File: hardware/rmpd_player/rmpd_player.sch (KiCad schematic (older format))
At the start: 63 parts, among them J1 POWER, J2 PROG, J3 LINE_OUT_INT, J4 LINE_OUT, J5 MICRO_SD, J6 POWER_INT, Q1 BC848, Q2 BC848, Q3 BC858, Q4 BC858, U1 DS3231M, U2 VS1011E, U3 LM1117-3.3, U4 ESP32-WROOM, Y1 12.288MHz

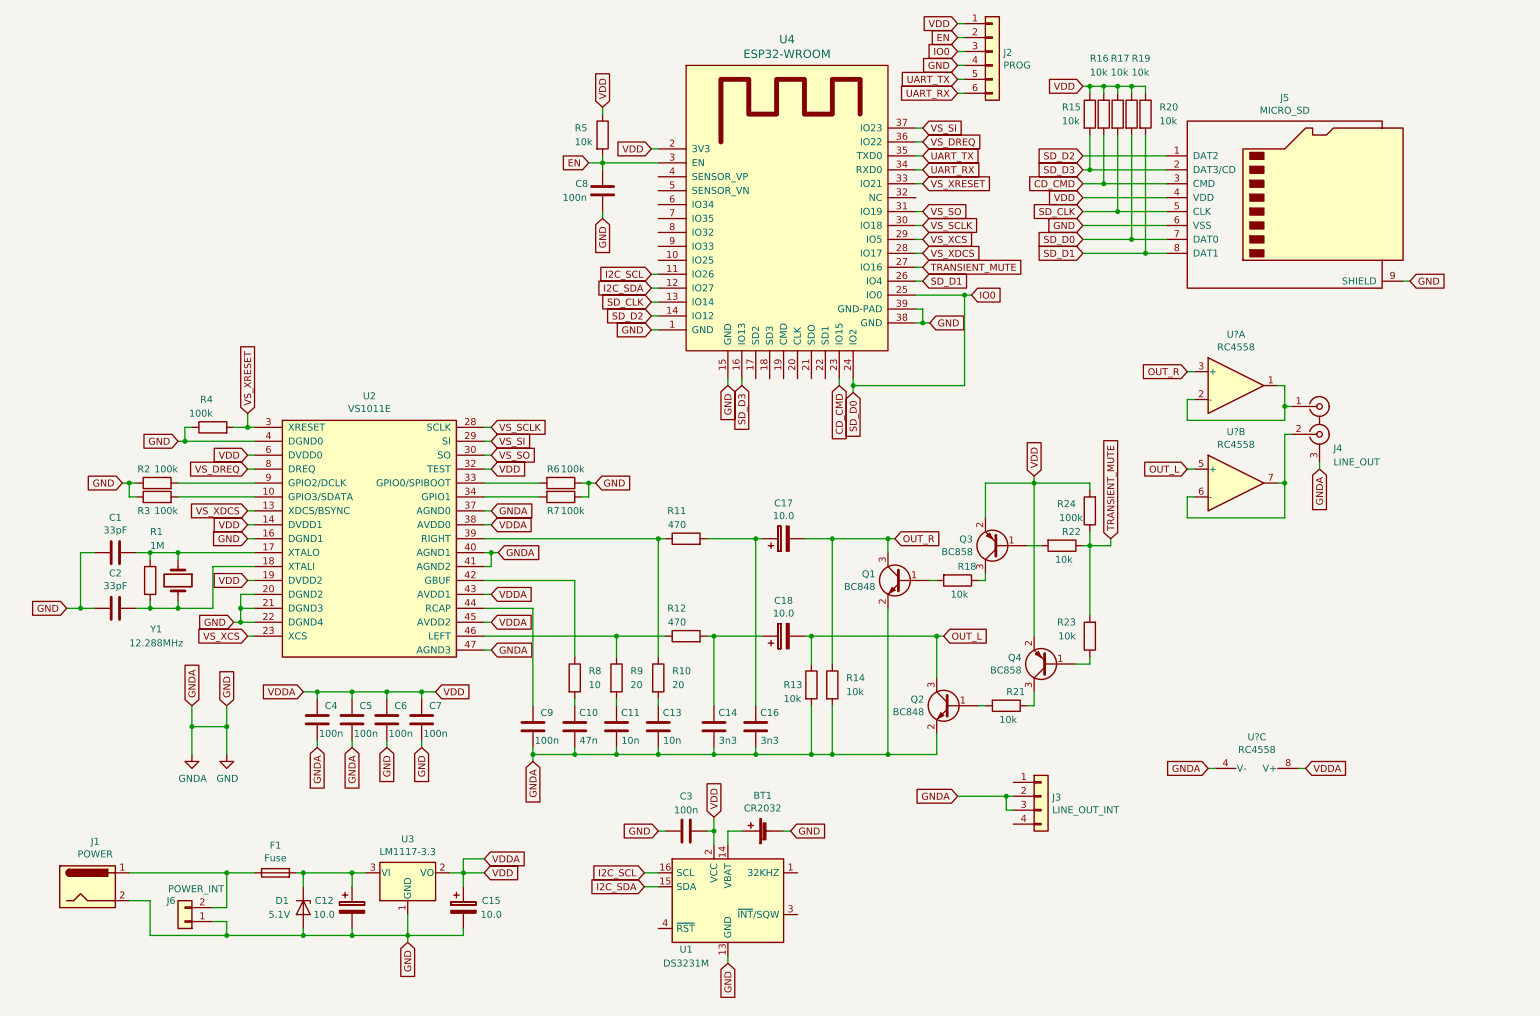
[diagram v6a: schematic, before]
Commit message: schematic op amp buffer; bom list
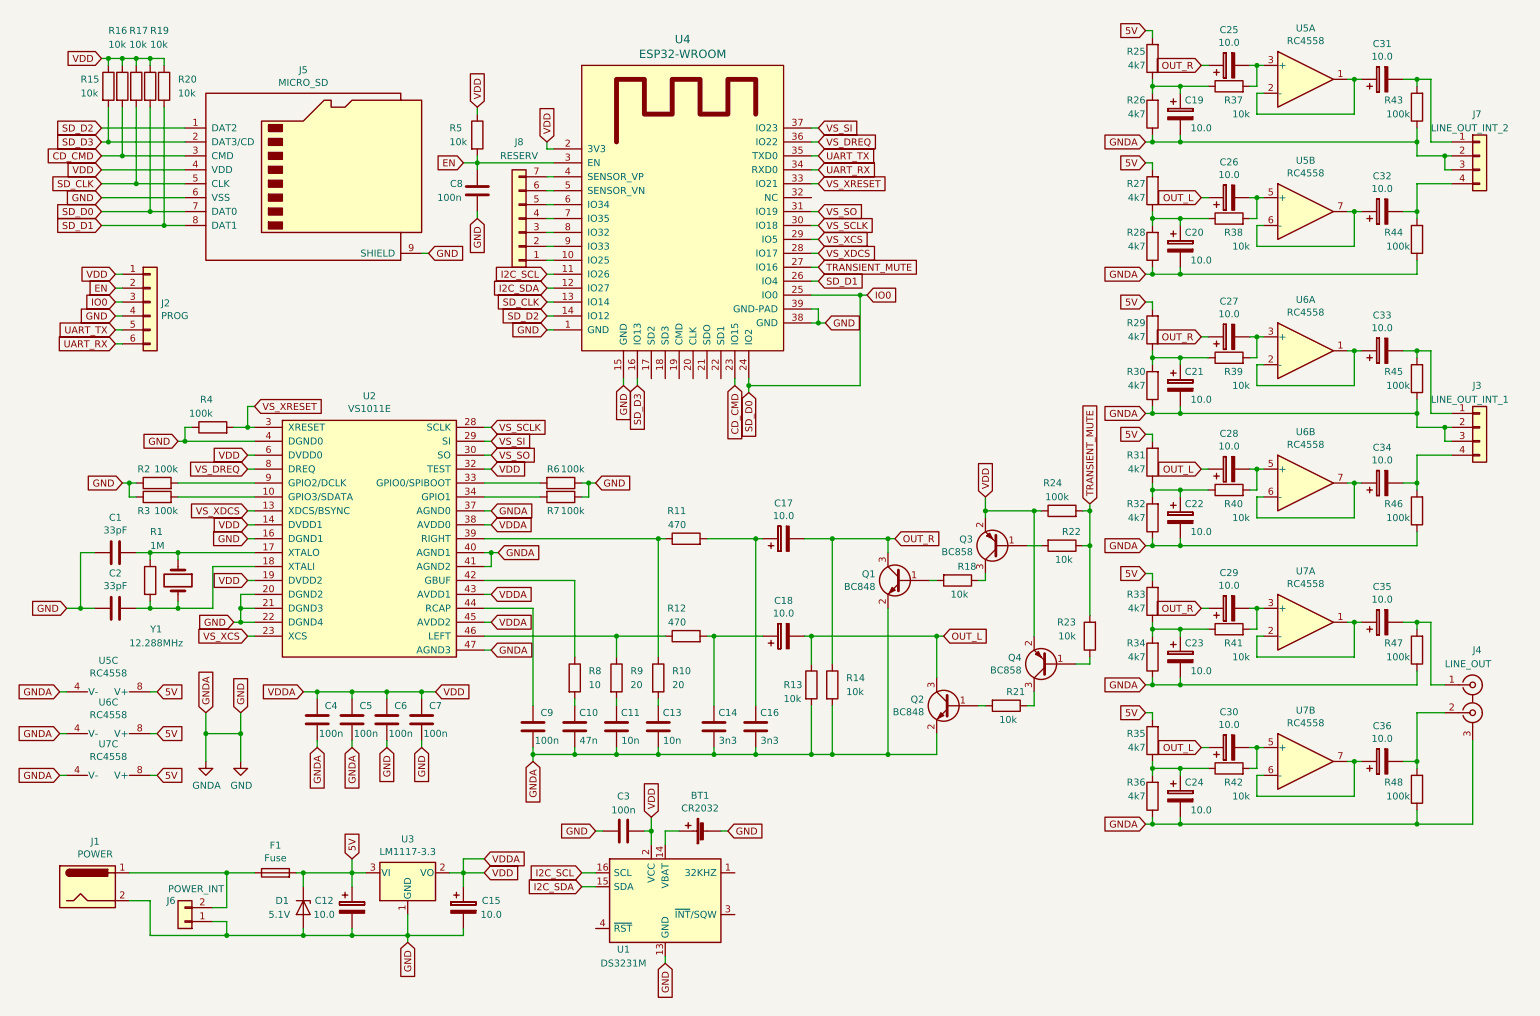
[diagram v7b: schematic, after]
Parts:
- added C19, C20, C21, C22, C23, C24, C25, C26, C27, C28, C29, C30, C31, C32, C33, C34, C35, C36: 10.0, Capacitors_THT:CP_Radial_D5.0mm_P2.50mm, symbol Device:CP
- added J7: LINE_OUT_INT_2, Pin_Headers:Pin_Header_Straight_1x04_Pitch2.54mm, symbol Connector_Generic:Conn_01x04
- added J8: RESERV, Pin_Headers:Pin_Header_Straight_1x07_Pitch2.54mm, symbol Connector_Generic:Conn_01x07
- added R25, R26, R27, R28, R29, R30, R31, R32, R33, R34, R35, R36: 4k7, Resistors_SMD:R_0805_HandSoldering, symbol Device:R
- added R37, R38, R39, R40, R41, R42: 10k, Resistors_SMD:R_0805_HandSoldering, symbol Device:R
- added R43, R44, R45, R46, R47, R48: 100k, Resistors_SMD:R_0805_HandSoldering, symbol Device:R
- added unit 1 of U5
- added unit 2 of U5
- added U6: RC4558, Power_Integrations:SO-8, symbol Amplifier_Operational:RC4558
- added unit 3 of U7
- J3: value LINE_OUT_INT -> LINE_OUT_INT_1
- U5, U7: renamed from U?; footprint (none) -> Power_Integrations:SO-8
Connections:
- net GND: now also C19.2, C20.2, C21.2, C22.2, C23.2, C24.2, J7.2 (Pin_2), J7.3 (Pin_3), R26.1, R28.1, R30.1, R32.1, R34.1, R36.1, R43.1, R44.1, R45.1, R46.1, R47.1, R48.1, U6.4 (V-), U7.4 (V-)
- net OUT_L: now also C26.1, C28.1, C30.1; no longer U7.5 (+)
- net OUT_R: now also C25.1, C27.1, C29.1; no longer U7.3 (+)
- net TRANSIENT_MUTE: now also R24.2; no longer R24.1
- net VDD: now also R24.1; no longer R24.2, U5.8 (V+)
- net at U4.10 (IO25): now also J8.1 (Pin_1)
- net at U4.4 (SENSOR_VP): now also J8.7 (Pin_7)
- net at U4.5 (SENSOR_VN): now also J8.6 (Pin_6)
- net at U4.6 (IO34): now also J8.5 (Pin_5)
- net at U4.7 (IO35): now also J8.4 (Pin_4)
- net at U4.8 (IO32): now also J8.3 (Pin_3)
- net at U4.9 (IO33): now also J8.2 (Pin_2)
- net 5V: now reaches C12.1, D1.1 (K), F1.2, U3.3 (VI)
- net 5V: now also U5.8 (V+), R25.2, R27.2, R29.2, R31.2, R33.2, R35.2, U6.8 (V+), U7.8 (V+)
- net at U7.1, U7.2 (-): now also C35.1; no longer J4.1 (IN1)
- net at U7.6 (-), U7.7: now also C36.1; no longer J4.2 (IN2)
- net at J3.1 (Pin_1): now also C33.2, R45.2
- net at J3.4 (Pin_4): now also C34.2, R46.2
- new net: C35.2, J4.1 (IN1), R47.2
- new net: C36.2, J4.2 (IN2), R48.2
- new net: C29.2, R41.2, U7.3 (+)
- new net: C30.2, R42.2, U7.5 (+)
- new net: C23.1, R33.1, R34.2, R41.1
- new net: C24.1, R35.1, R36.2, R42.1
- new net: C33.1, U6.1, U6.2 (-)
- new net: C27.2, R39.2, U6.3 (+)
- new net: C28.2, R40.2, U6.5 (+)
- new net: C34.1, U6.6 (-), U6.7
- new net: C21.1, R29.1, R30.2, R39.1
- new net: C22.1, R31.1, R32.2, R40.1
- new net: C31.2, J7.1 (Pin_1), R43.2
- new net: C32.2, J7.4 (Pin_4), R44.2
- new net: C31.1, U5.1, U5.2 (-)
- new net: C25.2, R37.2, U5.3 (+)
- new net: C26.2, R38.2, U5.5 (+)
- new net: C32.1, U5.6 (-), U5.7
- new net: C19.1, R25.1, R26.2, R37.1
- new net: C20.1, R27.1, R28.2, R38.1
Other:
- moved on the sheet: BT1, C3, C8, J2, J3, J4, J5, R15, R16, R17, R19, R20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

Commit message: op amps caps
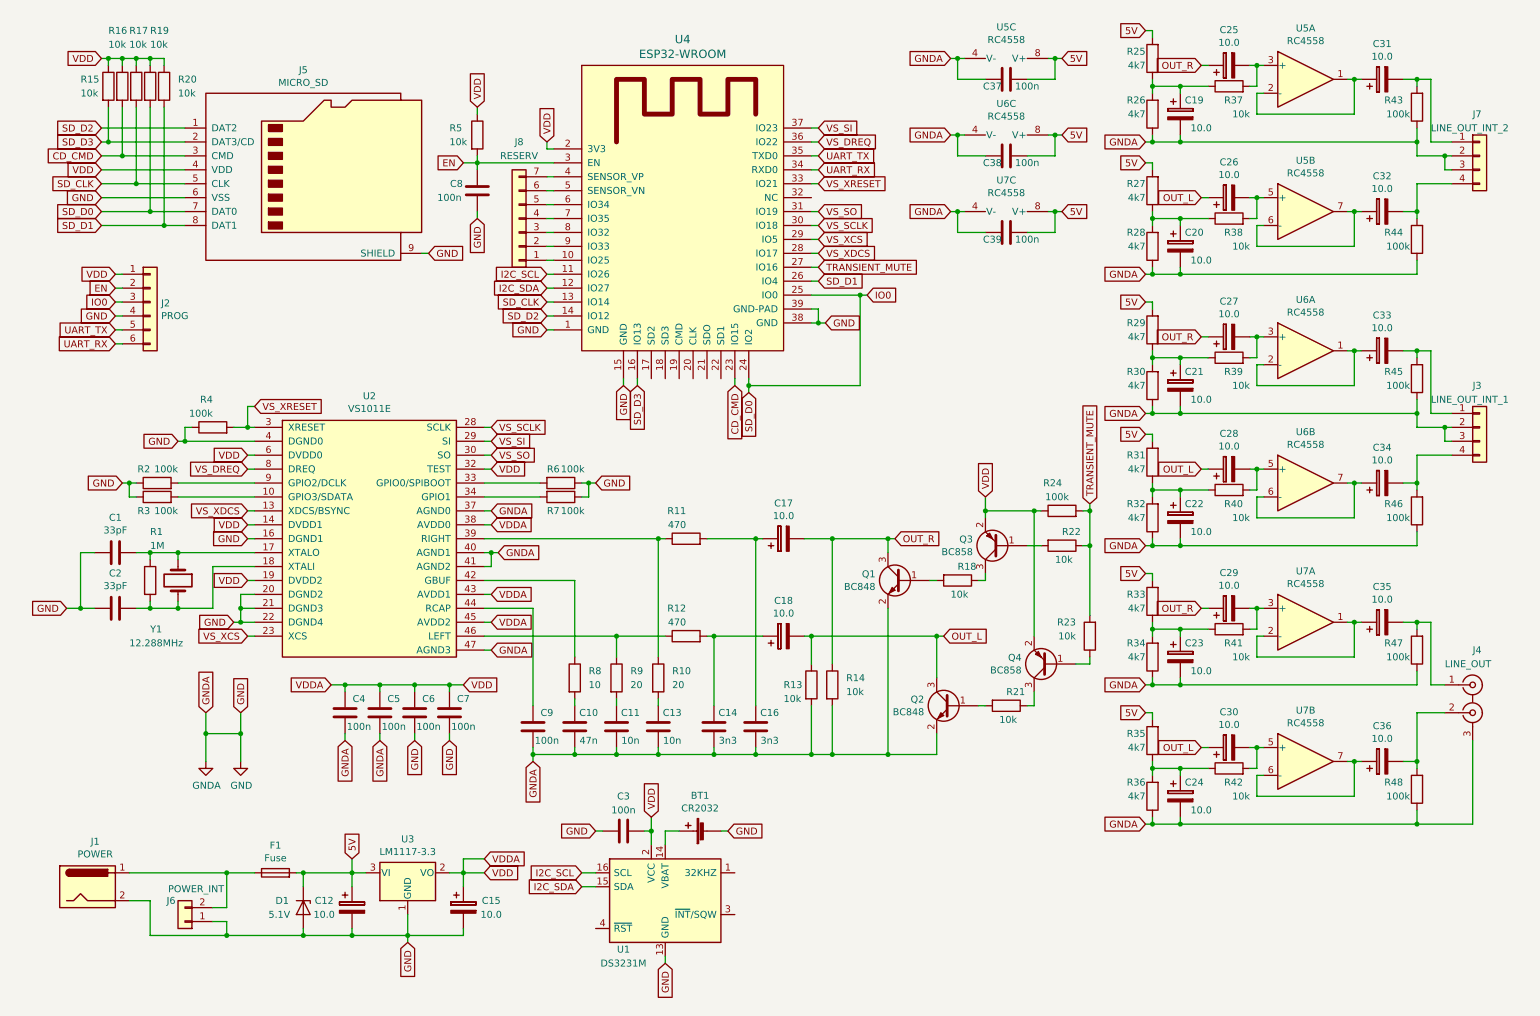
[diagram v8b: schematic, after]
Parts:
- added C37, C38, C39: 100n, Capacitors_SMD:C_0805_HandSoldering, symbol Device:C
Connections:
- net 5V: now also C37.1, C38.1, C39.1
- net GND: now also C37.2, C38.2, C39.2
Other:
- moved on the sheet: C4, C5, C6, C7, U5C, U6C, U7C
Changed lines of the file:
@@
 Wire Wire Line
 	6200 2350 6150 2350
-Text GLabel 2500 5500 0    50   Input ~ 0
+Text GLabel 2700 5450 0    50   Input ~ 0
 VDDA
-Text GLabel 3450 5500 2    50   Input ~ 0
+Text GLabel 3650 5450 2    50   Input ~ 0
 VDD
 $Comp
 L Device:C C4
 U 1 1 5C06DB73
-P 2600 5700
-F 0 "C4" H 2700 5800 50  0000 C CNN
-F 1 "100n" H 2700 5600 50  0000 C CNN
-F 2 "Capacitors_SMD:C_0805_HandSoldering" H 2638 5550 50  0001 C CNN
-F 3 "~" H 2600 5700 50  0001 C CNN
-	1    2600 5700
+P 2800 5650
+F 0 "C4" H 2900 5750 50  0000 C CNN
+F 1 "100n" H 2900 5550 50  0000 C CNN
+F 2 "Capacitors_SMD:C_0805_HandSoldering" H 2838 5500 50  0001 C CNN
+F 3 "~" H 2800 5650 50  0001 C CNN
+	1    2800 5650
 	1    0    0    -1
 $EndComp
@@
 L Device:C C7
 U 1 1 5C06DC75
-P 3350 5700
-F 0 "C7" H 3450 5800 50  0000 C CNN
-F 1 "100n" H 3450 5600 50  0000 C CNN
-F 2 "Capacitors_SMD:C_0805_HandSoldering" H 3388 5550 50  0001 C CNN
-F 3 "~" H 3350 5700 50  0001 C CNN
-	1    3350 5700
-	1    0    0    -1
-$EndComp
-Wire Wire Line
-	2500 5500 2600 5500
-Wire Wire Line
-	3350 5550 3350 5500
-Connection ~ 3350 5500
-Wire Wire Line
-	3350 5500 3450 5500
-Wire Wire Line
-	2600 5550 2600 5500
-Connection ~ 2600 5500
-Wire Wire Line
-	2600 5500 2850 5500
-Wire Wire Line
-	3350 5850 3350 5900
-Wire Wire Line
-	2600 5850 2600 5900
+P 3550 5650
+F 0 "C7" H 3650 5750 50  0000 C CNN
+F 1 "100n" H 3650 5550 50  0000 C CNN
+F 2 "Capacitors_SMD:C_0805_HandSoldering" H 3588 5500 50  0001 C CNN
+F 3 "~" H 3550 5650 50  0001 C CNN
+	1    3550 5650
+	1    0    0    -1
+$EndComp
+Wire Wire Line
+	2700 5450 2800 5450
+Wire Wire Line
+	3550 5500 3550 5450
+Connection ~ 3550 5450
+Wire Wire Line
+	3550 5450 3650 5450
+Wire Wire Line
+	2800 5500 2800 5450
+Connection ~ 2800 5450
+Wire Wire Line
+	2800 5450 3050 5450
+Wire Wire Line
+	3550 5800 3550 5850
+Wire Wire Line
+	2800 5800 2800 5850
 Wire Wire Line
 	3750 1700 4300 1700
-Text GLabel 3350 5900 3    50   Input ~ 0
+Text GLabel 3550 5850 3    50   Input ~ 0
 GND
-Text GLabel 2600 5900 3    50   Input ~ 0
+Text GLabel 2800 5850 3    50   Input ~ 0
 GNDA
 $Comp
@@
 L Device:C C5
 U 1 1 5C08CC4A
-P 2850 5700
-F 0 "C5" H 2950 5800 50  0000 C CNN
-F 1 "100n" H 2950 5600 50  0000 C CNN
-F 2 "Capacitors_SMD:C_0805_HandSoldering" H 2888 5550 50  0001 C CNN
-F 3 "~" H 2850 5700 50  0001 C CNN
-	1    2850 5700
+P 3050 5650
+F 0 "C5" H 3150 5750 50  0000 C CNN
+F 1 "100n" H 3150 5550 50  0000 C CNN
+F 2 "Capacitors_SMD:C_0805_HandSoldering" H 3088 5500 50  0001 C CNN
+F 3 "~" H 3050 5650 50  0001 C CNN
+	1    3050 5650
 	1    0    0    -1
 $EndComp
@@
 L Device:C C6
 U 1 1 5C08CCC0
-P 3100 5700
-F 0 "C6" H 3200 5800 50  0000 C CNN
-F 1 "100n" H 3200 5600 50  0000 C CNN
-F 2 "Capacitors_SMD:C_0805_HandSoldering" H 3138 5550 50  0001 C CNN
-F 3 "~" H 3100 5700 50  0001 C CNN
-	1    3100 5700
-	1    0    0    -1
-$EndComp
-Wire Wire Line
-	2850 5550 2850 5500
-Connection ~ 2850 5500
-Wire Wire Line
-	2850 5500 3100 5500
-Wire Wire Line
-	3100 5550 3100 5500
-Connection ~ 3100 5500
-Wire Wire Line
-	3100 5500 3350 5500
-Text GLabel 2850 5900 3    50   Input ~ 0
+P 3300 5650
+F 0 "C6" H 3400 5750 50  0000 C CNN
+F 1 "100n" H 3400 5550 50  0000 C CNN
+F 2 "Capacitors_SMD:C_0805_HandSoldering" H 3338 5500 50  0001 C CNN
+F 3 "~" H 3300 5650 50  0001 C CNN
+	1    3300 5650
+	1    0    0    -1
+$EndComp
+Wire Wire Line
+	3050 5500 3050 5450
+Connection ~ 3050 5450
+Wire Wire Line
+	3050 5450 3300 5450
+Wire Wire Line
+	3300 5500 3300 5450
+Connection ~ 3300 5450
+Wire Wire Line
+	3300 5450 3550 5450
+Text GLabel 3050 5850 3    50   Input ~ 0
 GNDA
-Text GLabel 3100 5900 3    50   Input ~ 0
+Text GLabel 3300 5850 3    50   Input ~ 0
 GND
 Wire Wire Line
-	2850 5850 2850 5900
-Wire Wire Line
-	3100 5850 3100 5900
+	3050 5800 3050 5850
+Wire Wire Line
+	3300 5800 3300 5850
 $Comp
 L Regulator_Linear:LM1117-3.3 U3
@@
 L Amplifier_Operational:RC4558 U5
 U 3 1 5C14ACCB
-P 1100 5600
-F 0 "U5" V 775 5600 50  0000 C CNN
-F 1 "RC4558" V 866 5600 50  0000 C CNN
-F 2 "Power_Integrations:SO-8" H 1100 5600 50  0001 C CNN
-F 3 "http://www.ti.com/lit/ds/symlink/rc4558.pdf" H 1100 5600 50  0001 C CNN
-	3    1100 5600
+P 7550 1050
+F 0 "U5" V 7225 1050 50  0000 C CNN
+F 1 "RC4558" V 7316 1050 50  0000 C CNN
+F 2 "Power_Integrations:SO-8" H 7550 1050 50  0001 C CNN
+F 3 "http://www.ti.com/lit/ds/symlink/rc4558.pdf" H 7550 1050 50  0001 C CNN
+	3    7550 1050
 	0    1    1    0
 $EndComp
@@
 Connection ~ 5050 4400
 Connection ~ 5050 5950
-Text GLabel 750  5500 0    50   Input ~ 0
+Text GLabel 7150 950  0    50   Input ~ 0
 GNDA
-Text GLabel 1450 5500 2    50   Input ~ 0
+Text GLabel 7950 950  2    50   Input ~ 0
 5V
 Wire Wire Line
-	750  5500 800  5500
-Wire Wire Line
-	1400 5500 1450 5500
+	7150 950  7200 950
+Wire Wire Line
+	7850 950  7900 950
 Wire Wire Line
 	9400 5100 9350 5100
@@
 L Amplifier_Operational:RC4558 U6
 U 3 1 5C5B9DB3
-P 1100 5900
-F 0 "U6" V 775 5900 50  0000 C CNN
-F 1 "RC4558" V 866 5900 50  0000 C CNN
-F 2 "Power_Integrations:SO-8" H 1100 5900 50  0001 C CNN
-F 3 "http://www.ti.com/lit/ds/symlink/rc4558.pdf" H 1100 5900 50  0001 C CNN
-	3    1100 5900
+P 7550 1600
+F 0 "U6" V 7225 1600 50  0000 C CNN
+F 1 "RC4558" V 7316 1600 50  0000 C CNN
+F 2 "Power_Integrations:SO-8" H 7550 1600 50  0001 C CNN
+F 3 "http://www.ti.com/lit/ds/symlink/rc4558.pdf" H 7550 1600 50  0001 C CNN
+	3    7550 1600
 	0    1    1    0
 $EndComp
-Text GLabel 750  5800 0    50   Input ~ 0
+Text GLabel 7150 1500 0    50   Input ~ 0
 GNDA
-Text GLabel 1450 5800 2    50   Input ~ 0
+Text GLabel 7950 1500 2    50   Input ~ 0
 5V
 Wire Wire Line
-	750  5800 800  5800
-Wire Wire Line
-	1400 5800 1450 5800
+	7150 1500 7200 1500
+Wire Wire Line
+	7850 1500 7900 1500
 Wire Wire Line
 	9400 3150 9350 3150
@@
 L Amplifier_Operational:RC4558 U7
 U 3 1 5D07BA24
-P 1100 6200
-F 0 "U7" V 775 6200 50  0000 C CNN
-F 1 "RC4558" V 866 6200 50  0000 C CNN
-F 2 "Power_Integrations:SO-8" H 1100 6200 50  0001 C CNN
-F 3 "http://www.ti.com/lit/ds/symlink/rc4558.pdf" H 1100 6200 50  0001 C CNN
-	3    1100 6200
+P 7550 2150
+F 0 "U7" V 7225 2150 50  0000 C CNN
+F 1 "RC4558" V 7316 2150 50  0000 C CNN
+F 2 "Power_Integrations:SO-8" H 7550 2150 50  0001 C CNN
+F 3 "http://www.ti.com/lit/ds/symlink/rc4558.pdf" H 7550 2150 50  0001 C CNN
+	3    7550 2150
 	0    1    1    0
 $EndComp
-Text GLabel 750  6100 0    50   Input ~ 0
+Text GLabel 7150 2050 0    50   Input ~ 0
 GNDA
-Text GLabel 1450 6100 2    50   Input ~ 0
+Text GLabel 7950 2050 2    50   Input ~ 0
 5V
 Wire Wire Line
-	750  6100 800  6100
-Wire Wire Line
-	1400 6100 1450 6100
+	7150 2050 7200 2050
+Wire Wire Line
+	7850 2050 7900 2050
 $Comp
 L Connector_Generic:Conn_01x07 J8
@@
 Wire Wire Line
 	4300 1800 4250 1800
+$Comp
+L Device:C C37
+U 1 1 5C262157
+P 7550 1100
+F 0 "C37" V 7600 1000 50  0000 C CNN
+F 1 "100n" V 7600 1250 50  0000 C CNN
+F 2 "Capacitors_SMD:C_0805_HandSoldering" H 7588 950 50  0001 C CNN
+F 3 "~" H 7550 1100 50  0001 C CNN
+	1    7550 1100
+	0    1    1    0
+$EndComp
+Wire Wire Line
+	7200 950  7200 1100
+Wire Wire Line
+	7200 1100 7400 1100
+Connection ~ 7200 950
+Wire Wire Line
+	7200 950  7250 950
+Wire Wire Line
+	7700 1100 7900 1100
+Wire Wire Line
+	7900 1100 7900 950
+Connection ~ 7900 950
+Wire Wire Line
+	7900 950  7950 950
+$Comp
+L Device:C C38
+U 1 1 5C429164
+P 7550 1650
+F 0 "C38" V 7600 1550 50  0000 C CNN
+F 1 "100n" V 7600 1800 50  0000 C CNN
+F 2 "Capacitors_SMD:C_0805_HandSoldering" H 7588 1500 50  0001 C CNN
+F 3 "~" H 7550 1650 50  0001 C CNN
+	1    7550 1650
+	0    1    1    0
+$EndComp
+$Comp
+L Device:C C39
+U 1 1 5C429358
+P 7550 2200
+F 0 "C39" V 7600 2100 50  0000 C CNN
+F 1 "100n" V 7600 2350 50  0000 C CNN
+F 2 "Capacitors_SMD:C_0805_HandSoldering" H 7588 2050 50  0001 C CNN
+F 3 "~" H 7550 2200 50  0001 C CNN
+	1    7550 2200
+	0    1    1    0
+$EndComp
+Wire Wire Line
+	7400 1650 7200 1650
+Wire Wire Line
+	7200 1650 7200 1500
+Connection ~ 7200 1500
+Wire Wire Line
+	7200 1500 7250 1500
+Wire Wire Line
+	7700 1650 7900 1650
+Wire Wire Line
+	7900 1650 7900 1500
+Connection ~ 7900 1500
+Wire Wire Line
+	7900 1500 7950 1500
+Wire Wire Line
+	7200 2050 7200 2200
+Wire Wire Line
+	7200 2200 7400 2200
+Connection ~ 7200 2050
+Wire Wire Line
+	7200 2050 7250 2050
+Wire Wire Line
+	7700 2200 7900 2200
+Wire Wire Line
+	7900 2200 7900 2050
+Connection ~ 7900 2050
+Wire Wire Line
+	7900 2050 7950 2050
 $EndSCHEMATC
